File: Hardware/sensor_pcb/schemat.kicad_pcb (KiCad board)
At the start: 2 copper layers, 116.8 x 22.2 mm, 42 parts, among them J7 SENSOR_CONN, J8 ToF Sensor

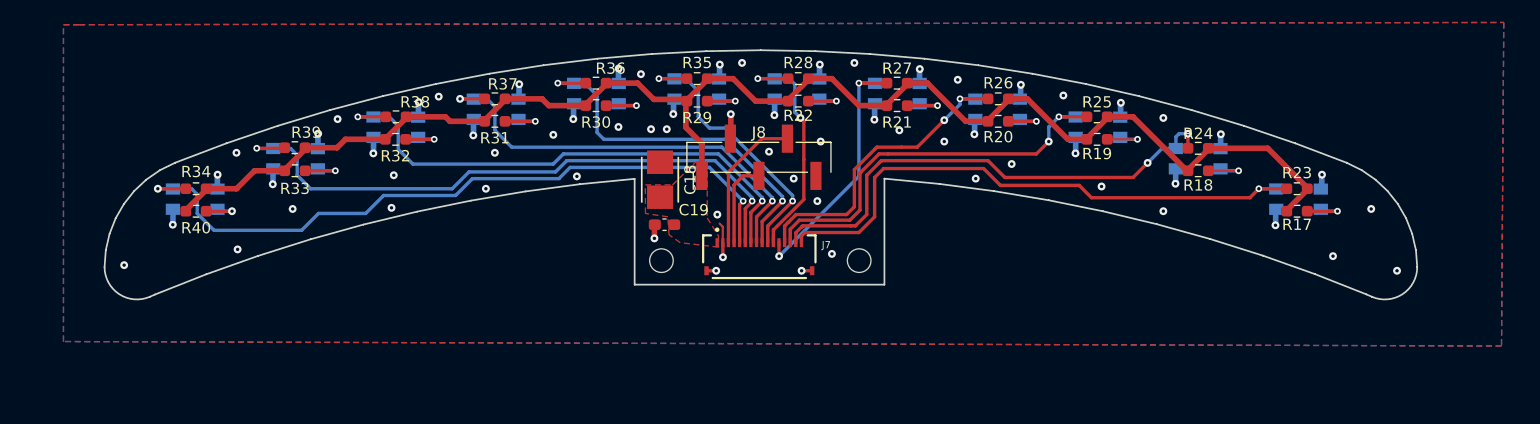
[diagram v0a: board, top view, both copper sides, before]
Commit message: PCB sensor layout updated
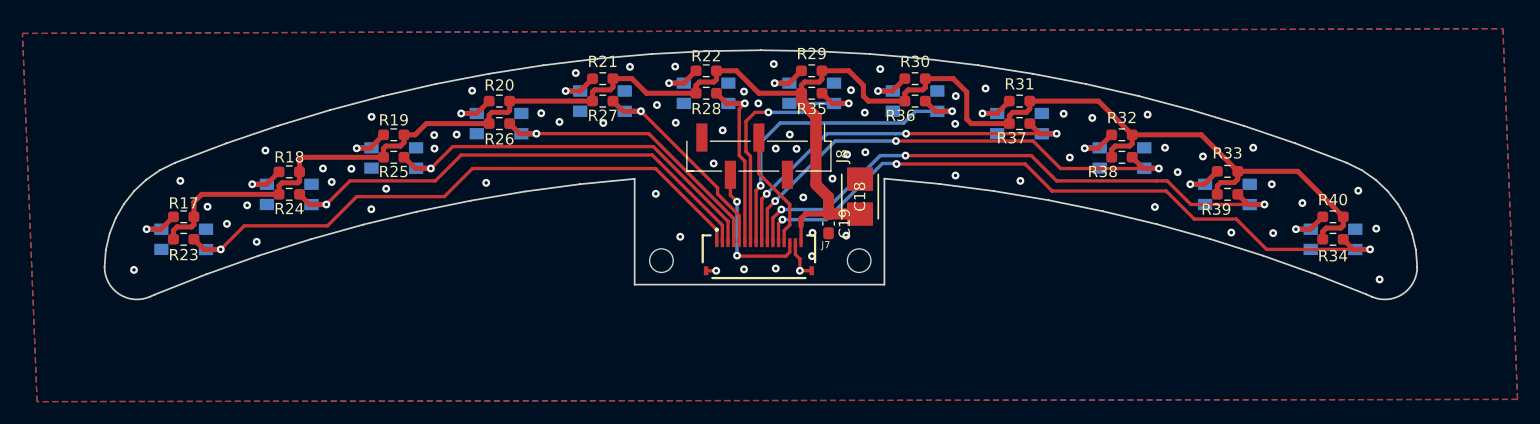
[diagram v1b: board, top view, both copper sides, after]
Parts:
- moved R40 101.3 mm to (197.6, 57.7), turned to 0 degrees
- moved R34 101.2 mm to (197.6, 55.7), turned to 180 degrees
- moved R23 99.2 mm to (95.3, 57.7), turned to 0 degrees
- moved R17 99.1 mm to (95.3, 55.7), turned to 180 degrees
- moved R39 83.1 mm to (188.2, 53.7), turned to 0 degrees
- moved R33 83.0 mm to (188.2, 51.6), turned to 180 degrees
- moved R24 81.0 mm to (104.7, 53.7), turned to 0 degrees
- moved R18 80.9 mm to (104.7, 51.7), turned to 180 degrees
- moved R38 64.7 mm to (178.8, 50.4), turned to 0 degrees
- moved R32 64.7 mm to (178.8, 48.4), turned to 180 degrees
- moved R25 62.7 mm to (114.0, 50.4), turned to 0 degrees
- moved R19 62.6 mm to (114.0, 48.4), turned to 180 degrees
- moved R37 46.8 mm to (169.7, 47.4), turned to 0 degrees
- moved R31 46.7 mm to (169.7, 45.4), turned to 180 degrees
- moved R26 44.5 mm to (123.4, 47.4), turned to 0 degrees
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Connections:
- CZ1 pad KOLEKTOR: /schemat_2/SENSOR1 -> /schemat_2/SENSOR12
- CZ10 pad KOLEKTOR: /schemat_2/SENSOR10 -> /schemat_2/SENSOR3
- CZ11 pad KOLEKTOR: /schemat_2/SENSOR11 -> /schemat_2/SENSOR2
- CZ12 pad KOLEKTOR: /schemat_2/SENSOR12 -> /schemat_2/SENSOR1
- CZ2 pad KOLEKTOR: /schemat_2/SENSOR2 -> /schemat_2/SENSOR11
- CZ3 pad KOLEKTOR: /schemat_2/SENSOR3 -> /schemat_2/SENSOR10
- CZ4 pad KOLEKTOR: /schemat_2/SENSOR4 -> /schemat_2/SENSOR9
- CZ5 pad KOLEKTOR: /schemat_2/SENSOR5 -> /schemat_2/SENSOR8
- CZ6 pad KOLEKTOR: /schemat_2/SENSOR6 -> /schemat_2/SENSOR7
- CZ7 pad KOLEKTOR: /schemat_2/SENSOR7 -> /schemat_2/SENSOR6
- CZ8 pad KOLEKTOR: /schemat_2/SENSOR8 -> /schemat_2/SENSOR5
- CZ9 pad KOLEKTOR: /schemat_2/SENSOR9 -> /schemat_2/SENSOR4
- J7 pad 1: +3.3V -> /schemat_2/SENSOR1
- J7 pad 10: /schemat_2/SENSOR7 -> /schemat_2/SENSOR10
- J7 pad 11: /schemat_2/SENSOR6 -> /schemat_2/SENSOR11
- J7 pad 12: /schemat_2/SENSOR5 -> /schemat_2/SENSOR12
- J7 pad 13: /schemat_2/SENSOR4 -> /schemat_2/I2C_SCL
- J7 pad 14: /schemat_2/SENSOR3 -> /schemat_2/I2C_SDA
- J7 pad 15: /schemat_2/SENSOR2 -> GND
- J7 pad 16: /schemat_2/SENSOR1 -> +3.3V
- J7 pad 2: GND -> /schemat_2/SENSOR2
- J7 pad 3: /schemat_2/I2C_SDA -> /schemat_2/SENSOR3
- J7 pad 4: /schemat_2/I2C_SCL -> /schemat_2/SENSOR4
- J7 pad 5: /schemat_2/SENSOR12 -> /schemat_2/SENSOR5
- J7 pad 6: /schemat_2/SENSOR11 -> /schemat_2/SENSOR6
- J7 pad 7: /schemat_2/SENSOR10 -> /schemat_2/SENSOR7
- J7 pad 8: /schemat_2/SENSOR9 -> /schemat_2/SENSOR8
- J7 pad 9: /schemat_2/SENSOR8 -> /schemat_2/SENSOR9
- R17 pad 2: Net-(CZ1-PadANODA) -> Net-(CZ12-PadANODA)
- R18 pad 2: Net-(CZ2-PadANODA) -> Net-(CZ11-PadANODA)
- R19 pad 2: Net-(CZ3-PadANODA) -> Net-(CZ10-PadANODA)
- R20 pad 2: Net-(CZ4-PadANODA) -> Net-(CZ9-PadANODA)
- R21 pad 2: Net-(CZ5-PadANODA) -> Net-(CZ8-PadANODA)
- R22 pad 2: Net-(CZ6-PadANODA) -> Net-(CZ7-PadANODA)
- R29 pad 2: Net-(CZ7-PadANODA) -> Net-(CZ6-PadANODA)
- R30 pad 2: Net-(CZ8-PadANODA) -> Net-(CZ5-PadANODA)
- R31 pad 2: Net-(CZ9-PadANODA) -> Net-(CZ4-PadANODA)
- R32 pad 2: Net-(CZ10-PadANODA) -> Net-(CZ3-PadANODA)
- R33 pad 2: Net-(CZ11-PadANODA) -> Net-(CZ2-PadANODA)
- R34 pad 2: Net-(CZ12-PadANODA) -> Net-(CZ1-PadANODA)
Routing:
- net +3.3V: track 129.5 -> 162.8 mm
- net GND: track 37.6 -> 4.64 mm, vias 65 -> 71
- net /schemat_2/SENSOR6: track 24.3 -> 17.2 mm, vias 2 -> 1
- net /schemat_2/SENSOR5: track 25.9 -> 19.6 mm, vias 2 -> 1
- net /schemat_2/SENSOR10: track 50.3 -> 44.1 mm, vias 2 -> 3
- net /schemat_2/SENSOR8: track 35.9 -> 30.0 mm
- net /schemat_2/SENSOR9: track 39.4 -> 35.2 mm, vias 2 -> 3
- net /schemat_2/SENSOR7: track 27.6 -> 23.6 mm
- net /schemat_2/SENSOR4: track 30.3 -> 26.9 mm, vias 2 -> 1
- net /schemat_2/SENSOR11: track 55.9 -> 52.7 mm, vias 2 -> 3
- net /schemat_2/I2C_SCL: track 7.68 -> 10.7 mm
- net Net-(CZ8-PadANODA): track 6.93 -> 4.13 mm
- net Net-(CZ5-PadANODA): track 6.95 -> 4.16 mm
- net Net-(CZ11-PadANODA): track 6.92 -> 4.15 mm
- net Net-(CZ1-PadANODA): track 6.84 -> 4.16 mm
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- removed copper zone on F.Cu, net +3.3V
